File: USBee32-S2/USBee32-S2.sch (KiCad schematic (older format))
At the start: 46 parts, among them J1 USB_A, J2 TYPE-C-31-M-12, J3 Conn_01x18_Male, J4 B2B-PH-SM4-TB(LF)(SN), J5 Conn_01x22_Male, Q1 MMBT8050, Q2 MMBT8050, SW1 SW_Push, SW2 SW_Push, U1 ESP32-S2-WROOM-ESP32-S2-WROOM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

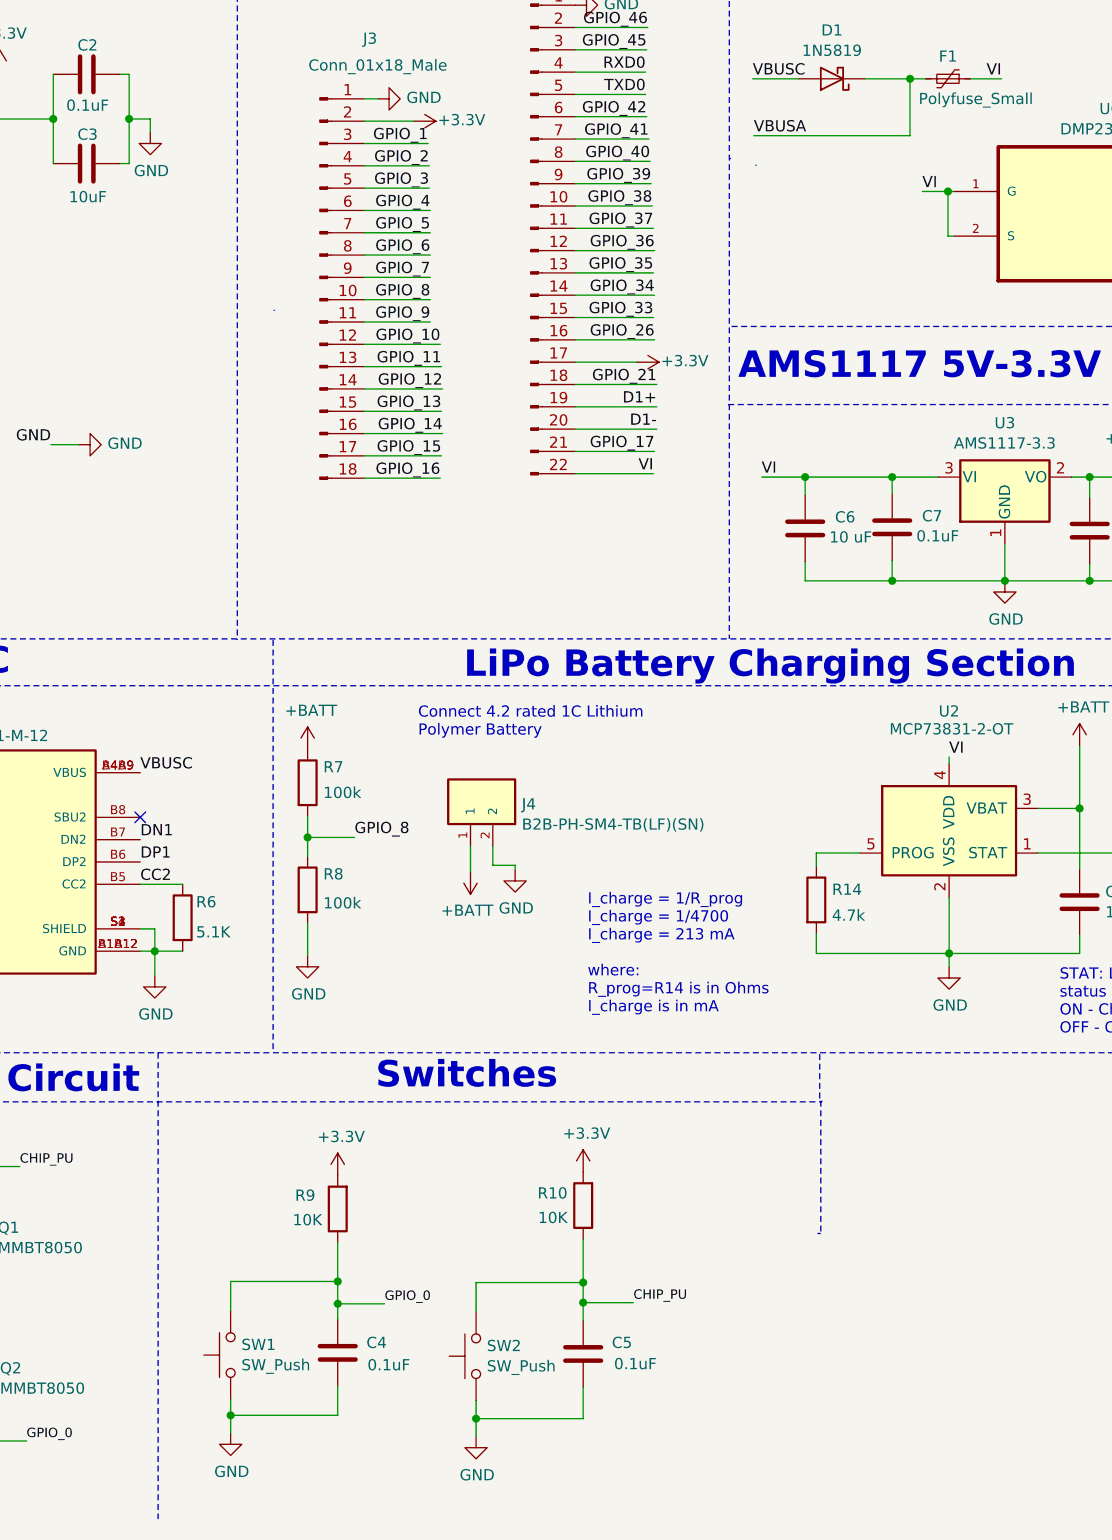
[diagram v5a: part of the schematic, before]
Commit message: Fixed Battery Charging Circuit
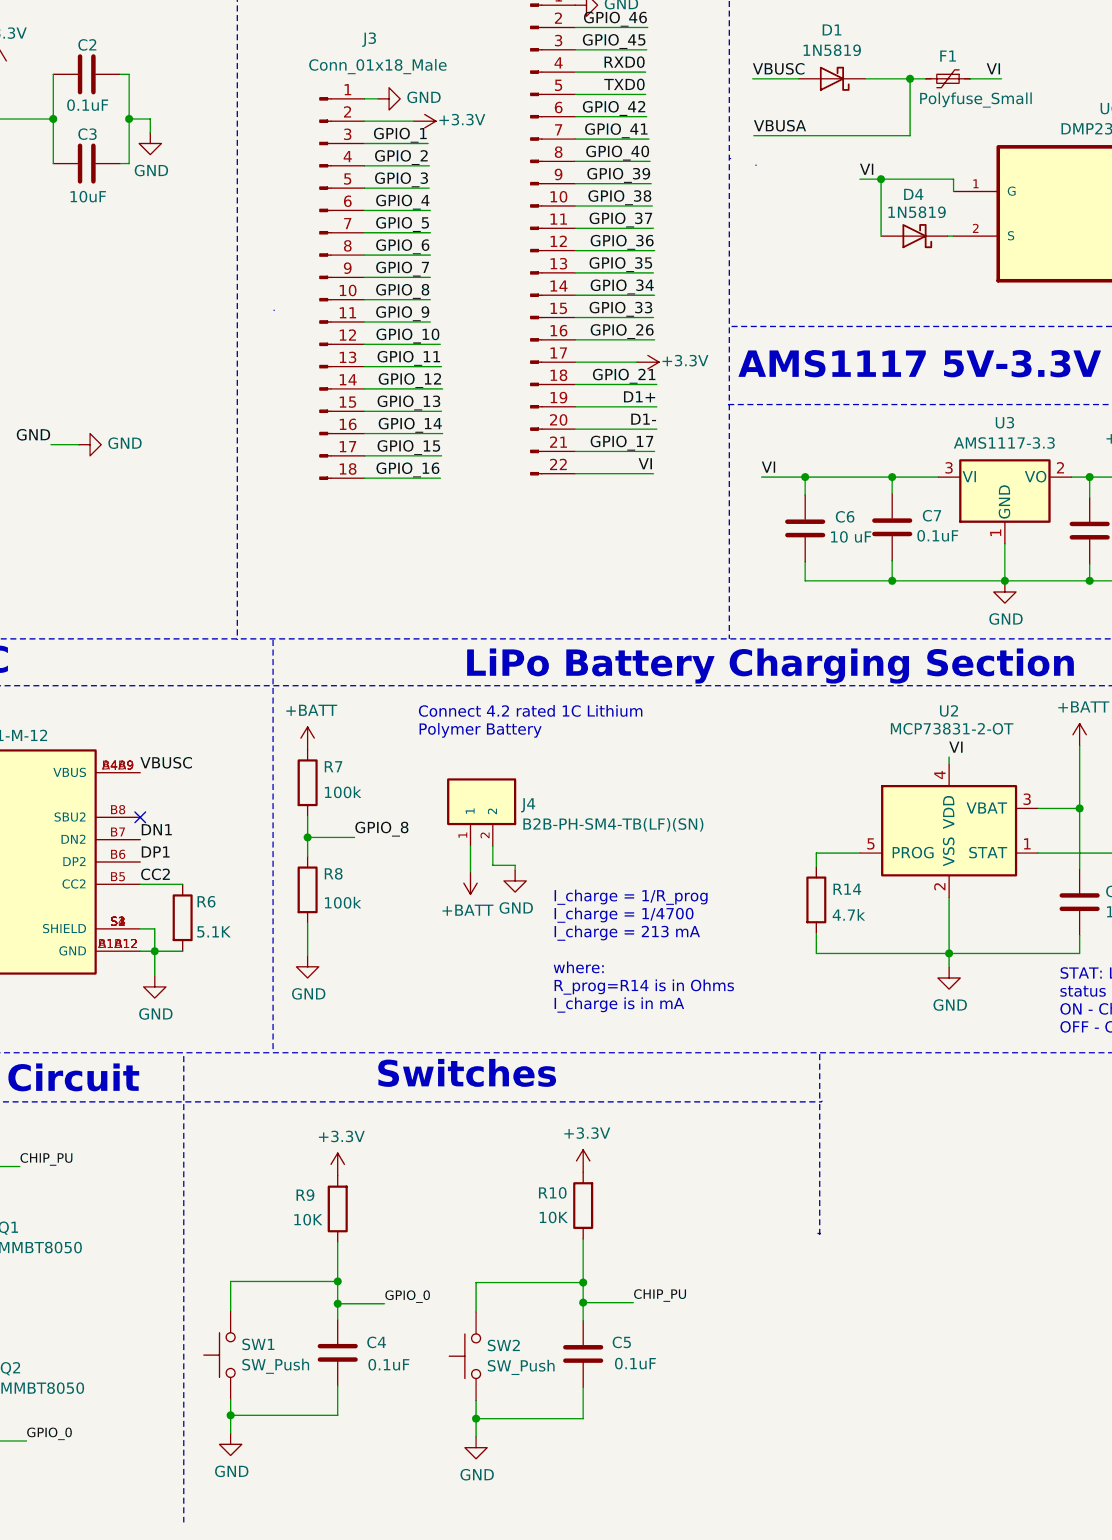
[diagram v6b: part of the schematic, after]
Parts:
- added D4: 1N5819, Diode_SMD:D_1206_3216Metric, symbol ESP32-S2-rescue:1N5819-Diode
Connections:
- net VI: now also D4.2 (A); no longer U6.2 (S)
- new net: D4.1 (K), U6.2 (S)
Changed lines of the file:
@@
 USB-C\n
 Wire Notes Line
-	4005 5710 4005 7800
+	4120 5725 4120 7815
 Wire Notes Line
 	4520 3860 4520 5710
@@
 USB Protection
 Wire Notes Line
-	6975 5925 6975 6520
+	6970 5940 6970 6535
 Wire Notes Line
 	6975 6520 6960 6520
@@
 Wire Wire Line
 	4675 4745 4675 4650
-Text Notes 5930 5540 0    50   ~ 0
+Text Notes 5775 5530 0    50   ~ 0
 I_charge = 1/R_prog\nI_charge = 1/4700 \nI_charge = 213 mA\n \nwhere:\nR_prog=R14 is in Ohms\nI_charge is in mA
 Wire Notes Line
@@
 	1    0    0    -1
 $EndComp
-Text Label 7430 1850 0    50   ~ 0
-VI
-Wire Wire Line
-	7570 1850 7545 1850
 Wire Wire Line
 	7570 2050 7545 2050
-Wire Wire Line
-	7545 2050 7545 1850
-Connection ~ 7545 1850
-Wire Wire Line
-	7545 1850 7430 1850
 Wire Wire Line
 	8970 1850 9030 1850
@@
 Text Notes 1990 5905 0    118  ~ 24
 Auto-Program Circuit\n
+$Comp
+L ESP32-S2-rescue:1N5819-Diode D4
+U 1 1 61664043
+P 7395 2050
+F 0 "D4" H 7400 1865 50  0000 C CNN
+F 1 "1N5819" H 7385 1945 50  0000 C CNN
+F 2 "Diode_SMD:D_1206_3216Metric" H 7395 1875 50  0001 C CNN
+F 3 "http://www.vishay.com/docs/88525/1n5817.pdf" H 7395 2050 50  0001 C CNN
+	1    7395 2050
+	-1   0    0    1
+$EndComp
+Wire Wire Line
+	7570 1850 7570 1795
+Wire Wire Line
+	7570 1795 7245 1795
+Connection ~ 7245 1795
+Wire Wire Line
+	7245 1795 7245 2050
+Wire Wire Line
+	7150 1795 7245 1795
+Text Label 7150 1795 0    50   ~ 0
+VI
 $EndSCHEMATC
